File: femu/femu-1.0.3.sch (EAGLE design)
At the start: 56 parts, among them IC1 ESP32-QFN_5X5

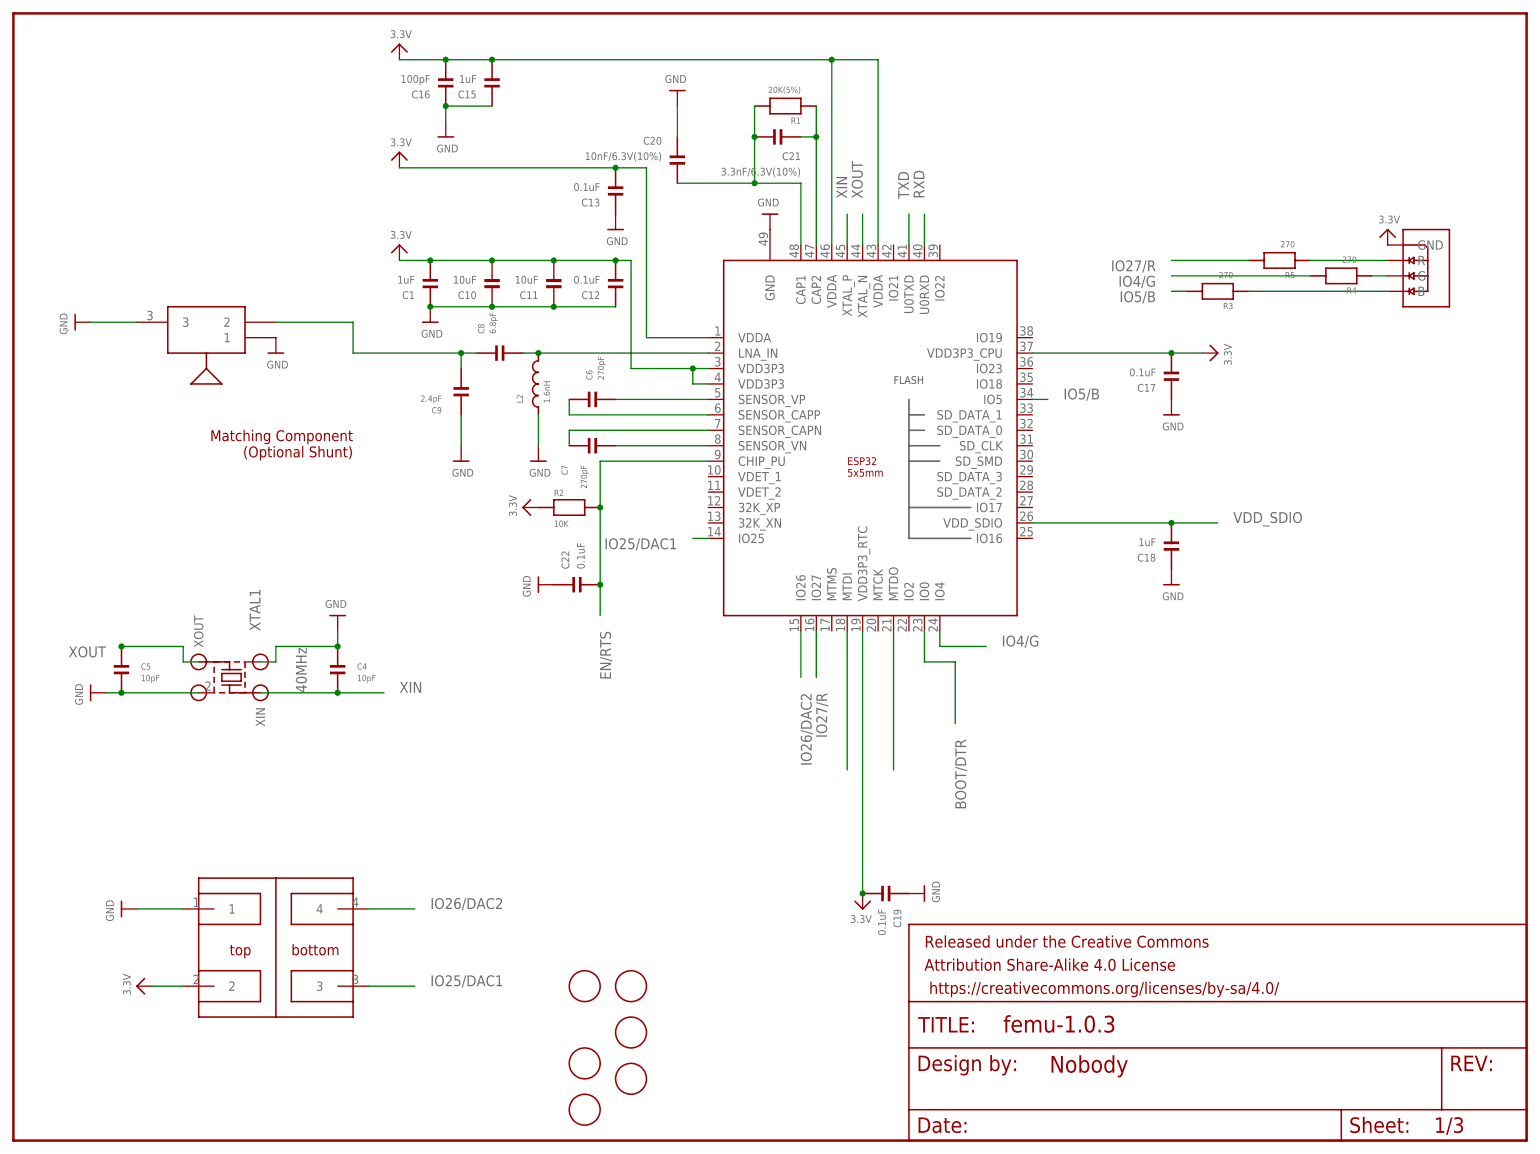
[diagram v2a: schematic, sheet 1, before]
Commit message: Adding current work on FEMU v1.0.3, which includes microvia adjustments
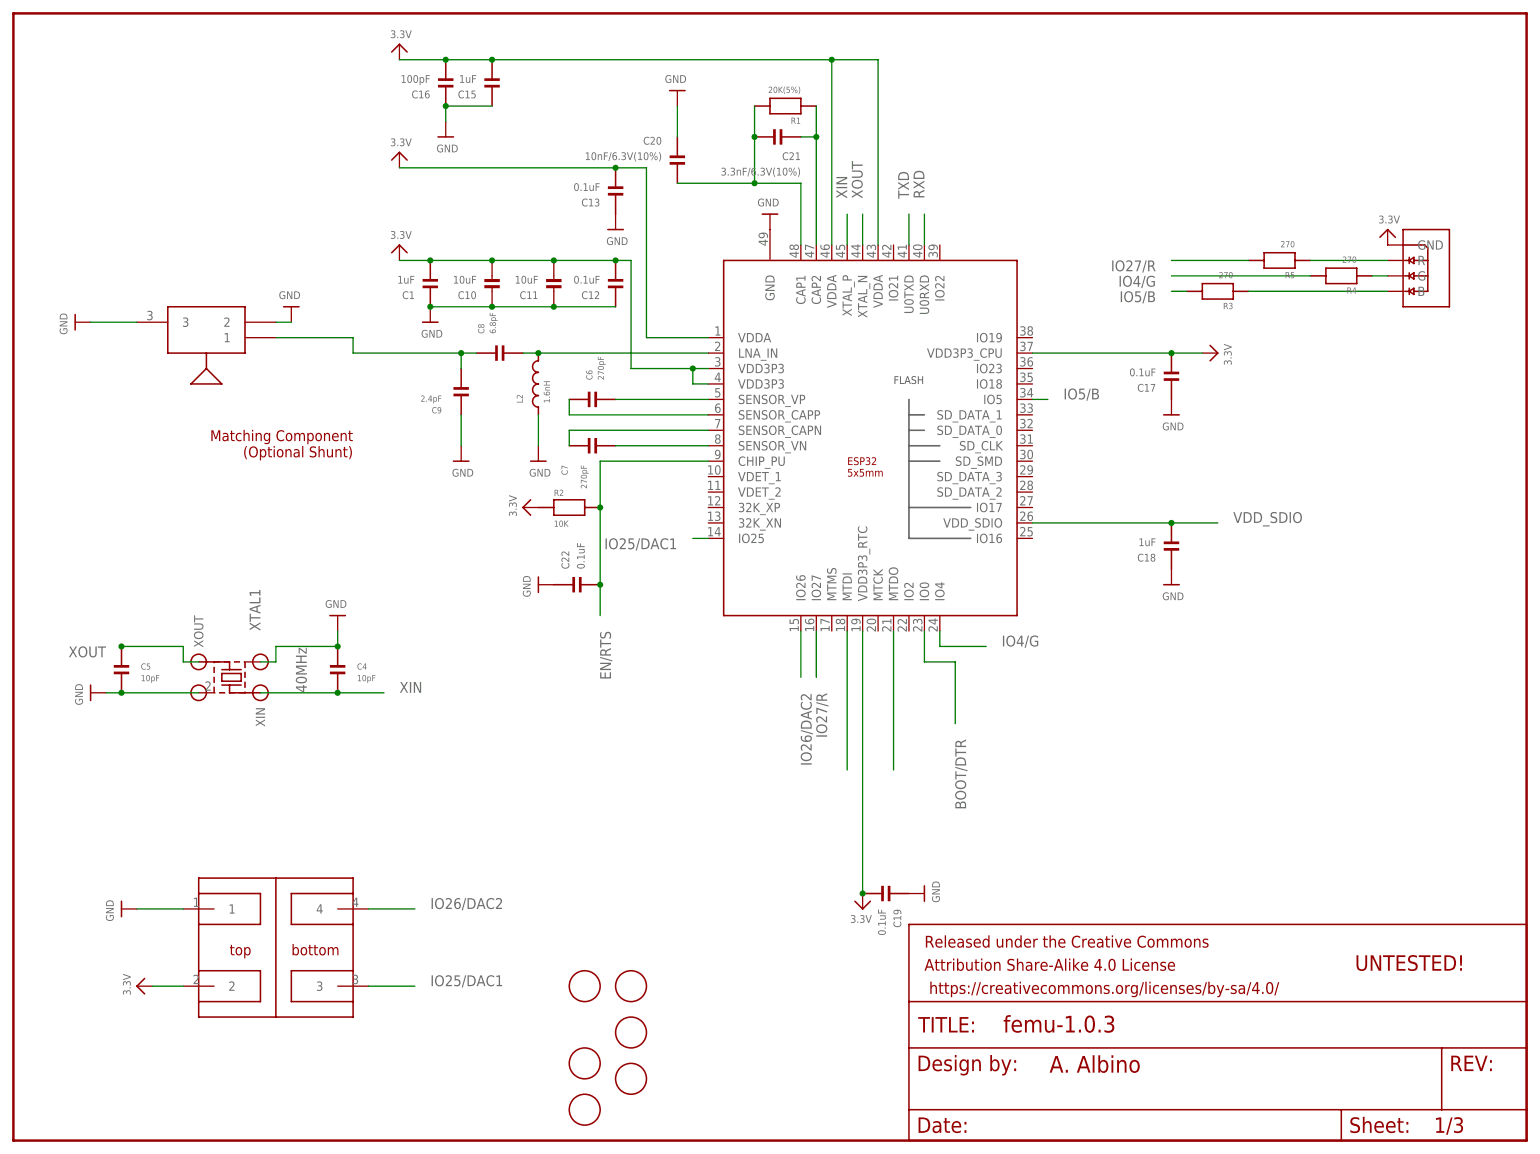
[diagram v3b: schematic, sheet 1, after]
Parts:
- FRAME1: DESIGNER (none) -> A. Albino; VERSION (none) -> v1.0.3
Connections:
- net GND: now also ANT1.2; no longer ANT1.1
- net N$6: now also ANT1.1; no longer ANT1.2
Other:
- note added: "UNTESTED!"
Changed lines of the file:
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@@
 <?xml version="1.0" encoding="utf-8"?>
 <!DOCTYPE eagle SYSTEM "eagle.dtd">
-<eagle version="9.3.2">
+<eagle version="9.6.1">
 <drawing>
 <settings>
@@
 </classes>
 <parts>
-<part name="FRAME1" library="SparkFun-Aesthetics" deviceset="FRAME-LETTER" device="NO_PACKAGE"/>
+<part name="FRAME1" library="SparkFun-Aesthetics" deviceset="FRAME-LETTER" device="NO_PACKAGE">
+<attribute name="DESIGNER" value="A. Albino"/>
+<attribute name="VERSION" value="v1.0.3"/>
+</part>
 <part name="IC1" library="esp32-wroom-32" deviceset="ESP32-QFN_5X5" device="">
 <attribute name="MPN" value="ESP32-D2WD"/>
@@
 <text x="55.88" y="116.84" size="1.778" layer="94" rot="R180">Matching Component
 (Optional Shunt)</text>
+<text x="238.76" y="30.48" size="2.54" layer="94" rot="R180">UNTESTED!</text>
 </plain>
 <instances>
@@
 <attribute name="VALUE" x="7.62" y="136.144" size="1.27" layer="96" rot="R270"/>
 </instance>
-<instance part="U$24" gate="G$1" x="43.18" y="129.54" smashed="yes">
-<attribute name="VALUE" x="41.656" y="127" size="1.27" layer="96"/>
+<instance part="U$24" gate="G$1" x="45.72" y="137.16" smashed="yes" rot="R180">
+<attribute name="VALUE" x="47.244" y="139.7" size="1.27" layer="96" rot="R180"/>
 </instance>
 <instance part="FID1" gate="G$1" x="93.98" y="25.4" smashed="yes"/>
@@
 </segment>
 <segment>
-<pinref part="ANT1" gate="G$1" pin="1"/>
 <pinref part="U$24" gate="G$1" pin="GND"/>
+<pinref part="ANT1" gate="G$1" pin="2"/>
+<wire x1="45.72" y1="134.62" x2="43.18" y2="134.62" width="0.1524" layer="91"/>
 </segment>
 </net>
@@
 <wire x1="76.2" y1="129.54" x2="73.66" y2="129.54" width="0.1524" layer="91"/>
 <junction x="73.66" y="129.54"/>
-<pinref part="ANT1" gate="G$1" pin="2"/>
-<wire x1="43.18" y1="134.62" x2="55.88" y2="134.62" width="0.1524" layer="91"/>
-<wire x1="55.88" y1="134.62" x2="55.88" y2="129.54" width="0.1524" layer="91"/>
+<pinref part="ANT1" gate="G$1" pin="1"/>
+<wire x1="55.88" y1="132.08" x2="55.88" y2="129.54" width="0.1524" layer="91"/>
+<wire x1="43.18" y1="132.08" x2="55.88" y2="132.08" width="0.1524" layer="91"/>
 </segment>
 </net>
